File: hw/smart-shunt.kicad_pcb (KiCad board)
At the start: 2 copper layers, 80.3 x 50.3 mm, 36 parts, among them J1 V supply, J2 V bus <80, J3 V bus >80, J4 Conn_01x01_Female, J5 Conn_01x01_Female, J6 GND, U1 XL7005A, U2 INA228, U3 ESP-12F

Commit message: finished pcb
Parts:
- removed C6: 0.1uF, Capacitor_SMD:C_0805_2012Metric
- removed D1: SS310, Diode_SMD:D_SMA_Handsoldering
- removed J5: Conn_01x01_Female, TestPoint:TestPoint_Loop_D3.50mm_Drill0.9mm_Beaded
- removed J6: GND, TestPoint:TestPoint_Loop_D3.50mm_Drill0.9mm_Beaded
- removed R10: 33k, Resistor_SMD:R_0805_2012Metric
- removed R8, R9: 10k, Resistor_SMD:R_0805_2012Metric
- removed U3: ESP-12F, RF_Module:ESP-12E
- added C10: 1uF 100V, Capacitor_SMD:C_0805_2012Metric, F.Cu at (81.0, 99.6)
- added C11: 100nF, Capacitor_SMD:C_0805_2012Metric, F.Cu at (127.3, 103.8)
- added C7: 0.1uF, Capacitor_SMD:C_0805_2012Metric, F.Cu at (100.9, 93.0)
- added H1: MountingHole, MountingHole:MountingHole_2.2mm_M2, F.Cu at (80.5, 73.8)
- added H2: MountingHole, MountingHole:MountingHole_2.2mm_M2, F.Cu at (80.6, 107.3)
- added H3: MountingHole, MountingHole:MountingHole_2.2mm_M2, F.Cu at (127.8, 107.3)
- added H4: MountingHole, MountingHole:MountingHole_2.2mm_M2, F.Cu at (127.9, 73.9)
- added J10: Conn_01x02_Pin, Connector_PinHeader_2.54mm:PinHeader_1x02_P2.54mm_Vertical, F.Cu at (81.2, 90.3)
- added J7: Screw_Terminal_01x01, open-pe:Wuerth_PowerPlus_M5_Nut, F.Cu at (91.4, 81.3)
- added J8: Screw_Terminal_01x01, open-pe:Wuerth_PowerPlus_M5_Nut, F.Cu at (119.4, 81.3)
- added JP3: Jumper_3_Open, Jumper:SolderJumper-3_P1.3mm_Open_RoundedPad1.0x1.5mm, F.Cu at (93.5, 93.4)
- added JP4: SolderJumper_2_Open, PCM_Resistor_SMD_AKL:R_0402_1005Metric, F.Cu at (109.7, 105.2)
- added JP5: SolderJumper_2_Open, PCM_Resistor_SMD_AKL:R_0402_1005Metric, F.Cu at (109.7, 103.9)
- added JP6: SolderJumper_2_Open, PCM_Resistor_SMD_AKL:R_0402_1005Metric, F.Cu at (109.7, 102.6)
- added L2: LBR2012T101K, Inductor_SMD:L_0805_2012Metric, F.Cu at (107.1, 96.3)
- added PS1: MIE1W0505BGLVH-3R-Z, open-pe:CONV_MIE1W0505BGLVH-3R-Z, F.Cu at (117.9, 98.0)
- added R15: 10, Resistor_SMD:R_0805_2012Metric, F.Cu at (96.7, 88.9)
- added R16: 100, Resistor_SMD:R_0805_2012Metric, F.Cu at (98.1, 92.1)
- added R17: 10k, Resistor_SMD:R_0805_2012Metric, F.Cu at (100.3, 98.0)
- added R18: R_Shunt, Resistor_SMD:R_Shunt_Isabellenhuette_BVR4026, F.Cu at (104.2, 81.3)
- added TH1: Thermistor_NTC, PCM_Resistor_SMD_AKL:R_0402_1005Metric, F.Cu at (104.1, 76.7)
- added TH2: Thermistor_NTC, PCM_Resistor_SMD_AKL:R_0402_1005Metric, F.Cu at (104.1, 80.5)
- added U4: TPT7721-SO1R, Package_SO:SOP-8_3.9x4.9mm_P1.27mm, F.Cu at (124.2, 92.1)
- C2: value 33nF -> 100nF
- C5: value 100uF -> 22uF; footprint Capacitor_SMD:CP_Elec_8x10 -> Capacitor_SMD:CP_Elec_6.3x5.9
- J1: value V supply -> Conn_01x03_Socket; footprint TestPoint:TestPoint_Loop_D3.50mm_Drill0.9mm_Beaded -> Connector_PinHeader_2.54mm:PinHeader_1x03_P2.54mm_Vertical
- J2: value V bus <80 -> UEXT_Slave; footprint TestPoint:TestPoint_Loop_D3.50mm_Drill0.9mm_Beaded -> Connector_PinHeader_2.54mm:PinHeader_2x05_P2.54mm_Vertical
- J3: value V bus >80 -> UEXT_Slave2; footprint TestPoint:TestPoint_Loop_D3.50mm_Drill0.9mm_Beaded -> Connector_PinHeader_2.54mm:PinHeader_2x05_P2.54mm_Vertical
- J4: value Conn_01x01_Female -> Conn_01x02_Pin; footprint TestPoint:TestPoint_Loop_D3.50mm_Drill0.9mm_Beaded -> Connector_PinHeader_2.54mm:PinHeader_1x02_P2.54mm_Vertical
- JP1: value Jumper_3_Bridged12 -> Jumper_2_Open; footprint Jumper:SolderJumper-3_P1.3mm_Bridged2Bar12_Pad1.0x1.5mm -> Jumper:SolderJumper-2_P1.3mm_Open_RoundedPad1.0x1.5mm
- JP2: value Jumper_2_Open -> SolderJumper_2_Open; footprint Jumper:SolderJumper-2_P1.3mm_Bridged2Bar_Pad1.0x1.5mm -> PCM_Resistor_SMD_AKL:R_0402_1005Metric
- L1: value 100uH -> 22uH; footprint Inductor_SMD:L_Taiyo-Yuden_NR-60xx_HandSoldering -> Inductor_SMD:L_0805_2012Metric
- R1, R2: footprint Resistor_SMD:R_0805_2012Metric -> Resistor_THT:R_Axial_DIN0204_L3.6mm_D1.6mm_P7.62mm_Horizontal
- R7: value 33k -> 10; footprint Resistor_SMD:R_0805_2012Metric -> PCM_Resistor_SMD_AKL:R_0805_2012Metric
- TP1, TP2, TP3: footprint TestPoint:TestPoint_Loop_D3.50mm_Drill0.9mm_Beaded -> TestPoint:TestPoint_Pad_D1.0mm
- U1: value XL7005A -> TPT72616-SO1R
- moved R3 62.6 mm to (87.6, 93.3), turned to 90 degrees
- moved R1 61.8 mm to (87.6, 97.1), turned to 90 degrees
- moved J1 58.6 mm to (82.8, 102.9), turned to 90 degrees
- moved R2 56.7 mm to (89.8, 89.5), turned to -90 degrees
- moved R4 56.6 mm to (89.8, 93.3), turned to -90 degrees
- moved JP1 53.7 mm to (93.5, 89.2), turned to -90 degrees
- moved L1 50.2 mm to (80.0, 102.7), turned to 90 degrees
- moved R7 44.6 mm to (80.4, 96.3), turned to 90 degrees
- moved J2 41.1 mm to (106.7, 102.9), turned to -90 degrees
- moved JP2 38.0 mm to (109.7, 106.4)
- moved TP3 36.3 mm to (99.9, 90.1)
- moved J4 34.1 mm to (91.9, 105.4), turned to 180 degrees
- moved J3 29.3 mm to (124.5, 102.9), turned to -90 degrees
- moved C2 24.5 mm to (118.4, 94.1), turned to 180 degrees
- moved R11 23.2 mm to (118.4, 91.9), turned to 180 degrees
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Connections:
- C1 pad 2: Net-(TP2-Pad1) -> Net-(JP1-B)
- C2 pad 2: Net-(C2-Pad2) -> GND
- C3 pad 1: +3.3V -> Net-(U2-VS)
- C4 pad 1: +3.3V -> Net-(U2-VS)
- C5 pad 2: Net-(C5-Pad2) -> GND
- D2 pad 2: Alert -> +3.3V
- J1 pad 1: Net-(U1-Pad1) -> Net-(J1-Pin_1)
- J2 pad 1: Vbus -> +3.3V
- J3 pad 1: Net-(J3-Pad1) -> +3.3V2
- J4 pad 1: Net-(J4-Pad1) -> Net-(J4-Pin_1)
- JP1 pad 1: Vbus -> Net-(JP1-A)
- JP1 pad 2: Net-(JP1-Pad2) -> Net-(JP1-B)
- JP2 pad 1: Net-(JP2-Pad1) -> A0
- JP2 pad 2: Vbus -> GND
- L1 pad 1: Net-(D1-Pad1) -> Net-(J1-Pin_1)
- L1 pad 2: +3.3V -> Net-(C10-Pad2)
- R1 pad 1: Net-(JP2-Pad1) -> Net-(JP3-A)
- R1 pad 2: Net-(J3-Pad1) -> Vin
- R2 pad 2: Net-(JP2-Pad1) -> Net-(JP3-A)
- R3 pad 1: Net-(JP2-Pad1) -> Net-(JP3-A)
- R3 pad 2: Net-(J3-Pad1) -> Vin
- R4 pad 2: Net-(JP2-Pad1) -> Net-(JP3-A)
- R5 pad 1: Net-(J4-Pad1) -> Shunt+
- R6 pad 1: Net-(J5-Pad1) -> Shunt-
- R6 pad 2: Net-(TP2-Pad1) -> Net-(JP1-B)
- R7 pad 1: +3.3V -> Net-(C10-Pad2)
- R7 pad 2: Net-(C2-Pad2) -> Vin
- TP2 pad 1: Net-(TP2-Pad1) -> Net-(JP1-B)
- TP3 pad 1: Vbus -> Net-(U2-Vbus)
- U1 pad 1: Net-(U1-Pad1) -> +3.3V2
- U1 pad 2: Net-(D1-Pad1) -> SDA2
- U1 pad 3: Net-(C2-Pad2) -> SCL2
- U1 pad 4: Net-(C5-Pad2) -> GND2
- U1 pad 5: Net-(C5-Pad2) -> GND
- U1 pad 6: Net-(C5-Pad2) -> SCL
- U1 pad 7: Net-(C5-Pad2) -> SDA
- U1 pad 8: Net-(C5-Pad2) -> +3.3V
- U2 pad 2: GND -> A0
- U2 pad 6: +3.3V -> Net-(U2-VS)
- U2 pad 8: Vbus -> Net-(U2-Vbus)
- U2 pad 9: Net-(TP2-Pad1) -> Net-(JP1-B)
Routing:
- net +3.3V: track 0.00 -> 81.9 mm
- net SCL: track 0.00 -> 60.2 mm, vias 0 -> 2
- net SDA: track 0.00 -> 44.8 mm, vias 0 -> 1
- net Alert: track 0.00 -> 39.3 mm, vias 0 -> 2
- net Net-(J4-Pin_1): track 0.00 -> 36.6 mm, vias 0 -> 2
- net GND2: track 0.00 -> 33.9 mm
- net Net-(J4-Pin_2): track 0.00 -> 32.2 mm, vias 0 -> 1
- net +3.3V2: track 0.00 -> 28.2 mm
- net GND: track 0.00 -> 23.2 mm, vias 0 -> 3
- net Vin: track 0.00 -> 21.7 mm
- net Net-(JP1-B): track 0.00 -> 20.7 mm, vias 0 -> 2
- net A0: track 0.00 -> 14.9 mm, vias 0 -> 2
- net Alert2: track 0.00 -> 12.2 mm
- net SDA2: track 0.00 -> 11.4 mm, vias 0 -> 1
- net Net-(JP3-A): track 0.00 -> 10.6 mm
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- added copper zone on F.Cu, net GND
- added copper zone on B.Cu, net P+
- added copper zone on F.Cu, net P+
- added copper zone on B.Cu, net P-
- added copper zone on F.Cu, net P-
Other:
- board size 80.3 x 50.3 mm -> 50.8 x 37.1 mm
- board text added: "00"
- board text added: "01"
- board text added: "10"
- board text added: "11"
- board text added: "3.3V PSU"
- board text added: "NTC 10k"
- board text added: "UEXT (I2C)"
- board text added: "UEXT isolated"
- board text added: "i2c addr 100000xx"
- board text removed: "use double footprints for resistors (THT and SMD) add filter connectors"

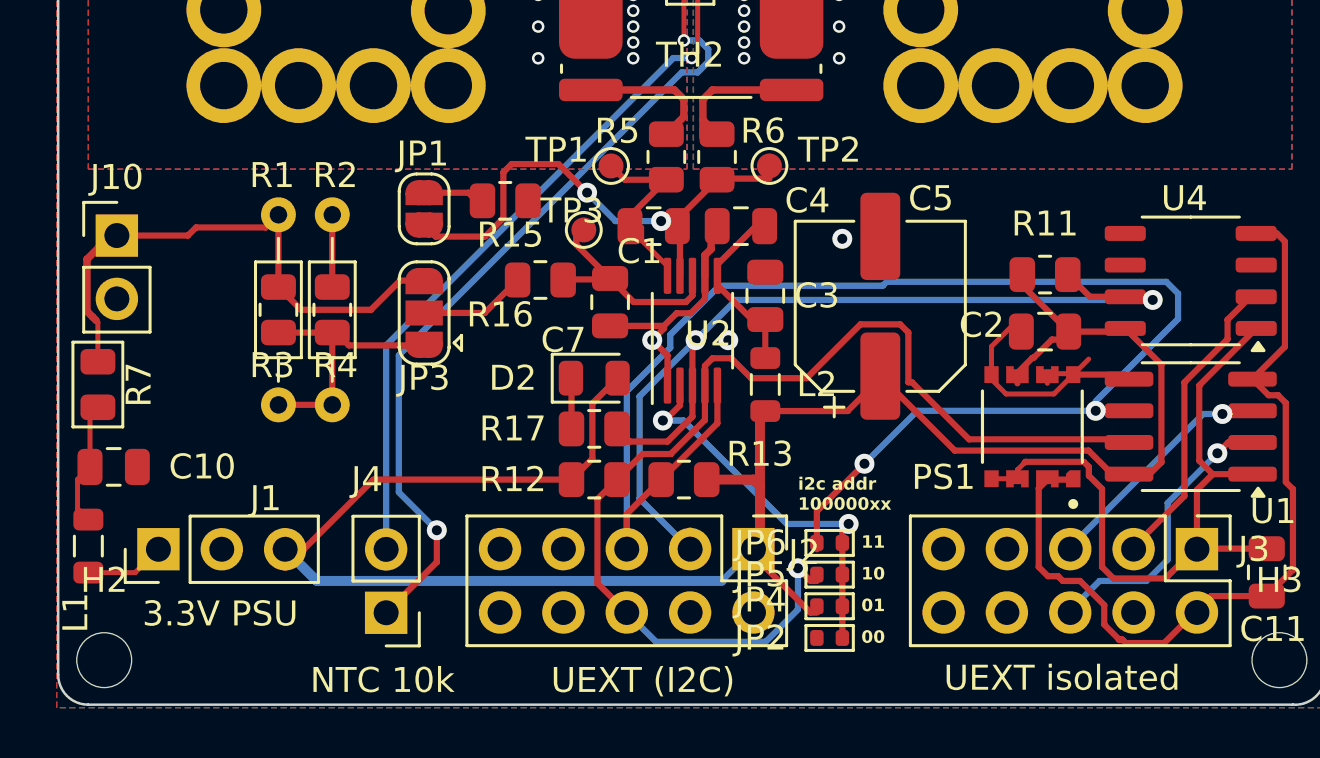
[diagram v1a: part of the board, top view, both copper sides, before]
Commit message: add battery connector and LDO
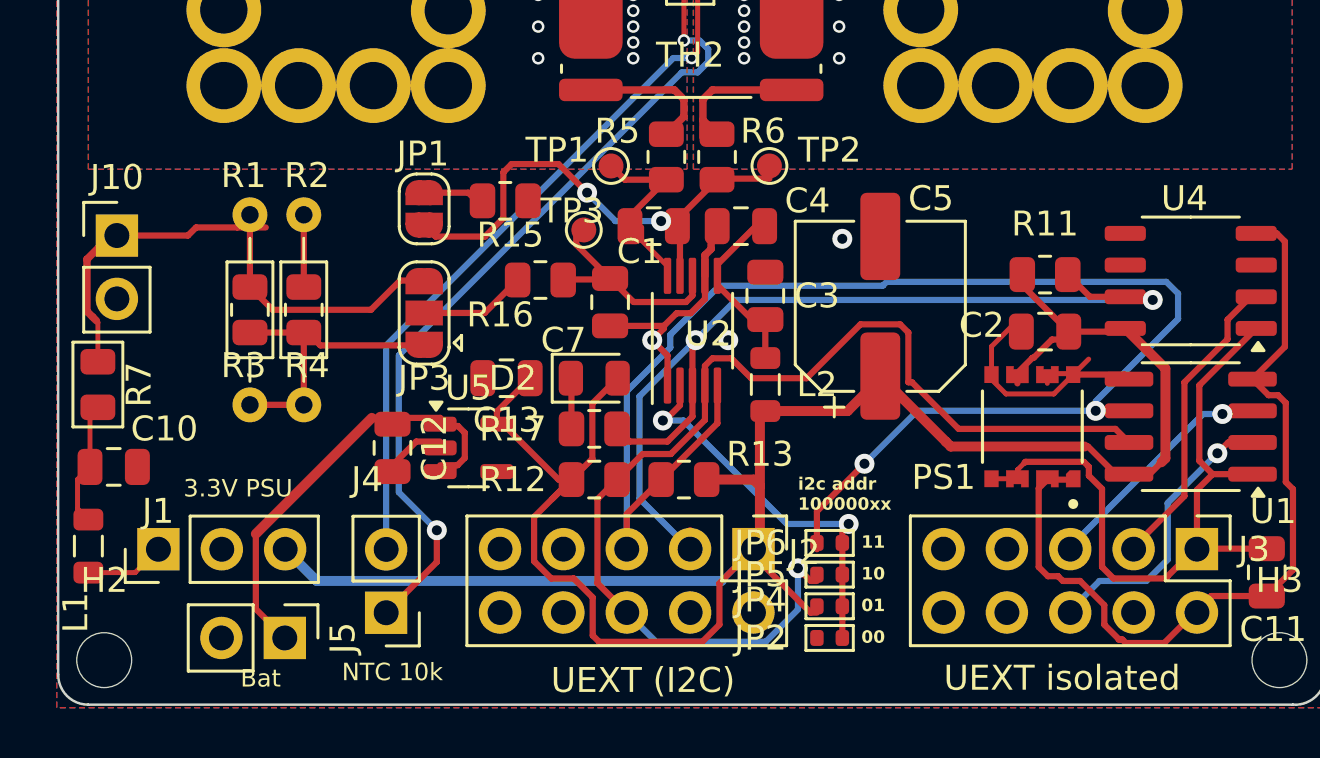
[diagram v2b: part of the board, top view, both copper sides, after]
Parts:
- added C12: 100nF, Capacitor_SMD:C_0805_2012Metric, F.Cu at (92.2, 98.8)
- added C13: 100nF, Capacitor_SMD:C_0805_2012Metric, F.Cu at (96.8, 96.0)
- added J5: Conn_01x02_Pin, Connector_PinHeader_2.54mm:PinHeader_1x02_P2.54mm_Vertical, F.Cu at (87.9, 106.4)
- added U5: TLV74033PDBVR, Package_TO_SOT_SMD:SOT-23-5, F.Cu at (95.2, 98.8)
- moved R1 1.14 mm to (86.5, 97.1)
- moved R2 1.14 mm to (88.6, 89.5)
- moved R3 1.14 mm to (86.5, 93.3)
- moved R4 1.14 mm to (88.6, 93.3)
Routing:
- net Net-(J5-Pin_1): track 0.00 -> 17.3 mm
- net +3.3V: track 81.9 -> 94.0 mm
- net GND: track 23.2 -> 25.5 mm
- net Vin: track 21.7 -> 22.8 mm
- net Net-(JP3-A): track 10.6 -> 11.7 mm
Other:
- board text added: "Bat"

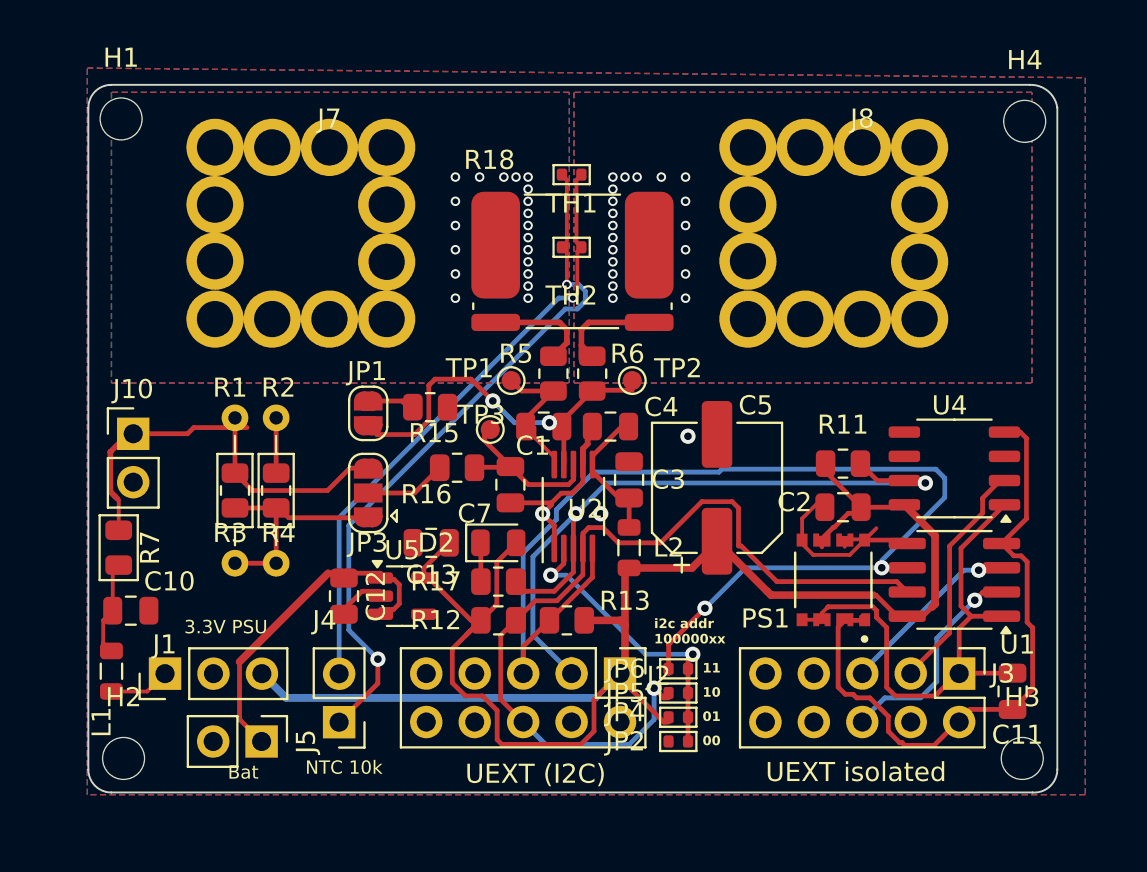
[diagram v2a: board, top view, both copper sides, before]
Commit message: hw: 2nd LDO, mounting holes
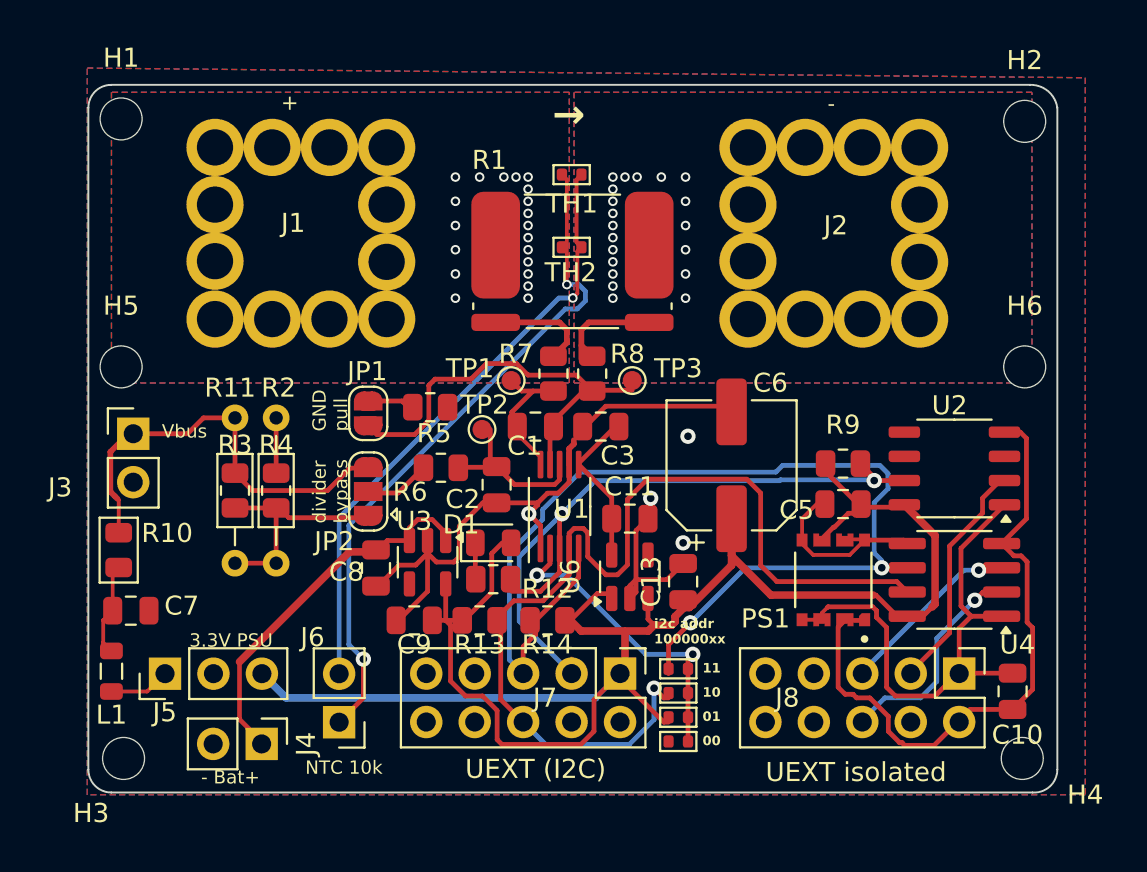
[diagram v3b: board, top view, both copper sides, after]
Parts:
- removed the C3 at (107.1, 92.7)
- removed L2: LBR2012T101K, Inductor_SMD:L_0805_2012Metric
- added C11: 1uF, Capacitor_SMD:C_0805_2012Metric, F.Cu at (107.2, 94.7)
- added C13: 1uF, Capacitor_SMD:C_0805_2012Metric, F.Cu at (110.0, 98.0)
- added H5: MountingHole, MountingHole:MountingHole_2.2mm_M2, F.Cu at (80.5, 86.8)
- added H6: MountingHole, MountingHole:MountingHole_2.2mm_M2, F.Cu at (127.9, 86.8)
- added U6: TLV74130PDBVR, Package_TO_SOT_SMD:SOT-23-5, F.Cu at (107.2, 97.8)
- C1: value 0.1uF -> 100nF
- C2: renamed from C7; value 0.1uF -> 100nF, 100V
- C3: renamed from C4; value 0.1uF -> 100nF
- moved R13 4.57 mm to (99.3, 100.1)
- moved C9 4.16 mm to (95.9, 100.1)
- moved R14 2.58 mm to (102.9, 100.1)
- moved C8 2.23 mm to (93.9, 97.3)
- moved U3 2.22 mm to (96.6, 97.0), turned to -90 degrees
- moved C6 1.40 mm to (112.5, 91.9)
- moved R6 0.85 mm to (97.3, 92.1)
- moved C2 0.72 mm to (100.2, 93.0)
- moved U1 0.72 mm to (103.5, 94.1)
- moved C3 0.51 mm to (105.7, 89.9)
- moved C1 0.44 mm to (102.2, 89.9)
- moved TP2 0.43 mm to (99.4, 90.1)
- moved R12 0.30 mm to (100.0, 97.9)
- moved D1 0.27 mm to (100.0, 96.0)
- moved C5 0.16 mm to (118.4, 94.0)
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- renumbered C11 to C10, C2 to C5, C5 to C6, C10 to C7, C12 to C8, C13 to C9, D2 to D1, H4 to H2, H2 to H3, H3 to H4, J7 to J1, J8 to J2, J10 to J3, J5 to J4, J1 to J5, J4 to J6, J2 to J7, J3 to J8, JP3 to JP2, JP4 to JP3, JP2 to JP4, JP6 to JP5, JP5 to JP6, R18 to R1, R7 to R10, R1 to R11, R17 to R12, R12 to R14, R15 to R5, R16 to R6, R5 to R7, R6 to R8, R11 to R9, TP3 to TP2, TP2 to TP3, U2 to U1, U4 to U2, U5 to U3, U1 to U4
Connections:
- net Net-(U2-VS) renamed +3V
- R13 pad 1: +3.3V -> SDA
- R13 pad 2: SCL -> +3.3V
- R14 pad 1: SDA -> +3.3V
- R14 pad 2: +3.3V -> SCL
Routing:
- net GND: track 25.5 -> 54.1 mm, vias 3 -> 4
- net SDA: track 44.8 -> 51.8 mm
- net SCL: track 60.2 -> 57.4 mm
- net +3.3V: track 94.0 -> 96.8 mm
- net Net-(J4-Pin_1): track 17.3 -> 20.1 mm
- net Alert: track 39.3 -> 37.1 mm
- net Net-(JP1-B): track 20.7 -> 22.7 mm, vias 2 -> 0
- net +3V: track 7.42 -> 8.62 mm
- net Vin: track 22.8 -> 21.7 mm
- net Vbus: track 3.79 -> 2.94 mm
- net A0: track 14.9 -> 15.6 mm
- net Net-(J6-Pin_1): track 36.6 -> 35.9 mm
- net Net-(U1-Vbus): track 9.16 -> 8.58 mm
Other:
- board text added: "+"
- board text added: "-"
- board text added: "- Bat+"
- board text added: "GND pull"
- board text added: "Vbus"
- board text added: "divider bypass"
- board text added: "→"
- board text removed: "Bat"

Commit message: etc
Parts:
- added J10: Conn_01x01, Connector_PinHeader_2.54mm:PinHeader_1x01_P2.54mm_Vertical, F.Cu at (100.4, 85.9)
- added J11: Conn_01x01, Connector_PinHeader_2.54mm:PinHeader_1x01_P2.54mm_Vertical, F.Cu at (107.9, 85.9)
- added JP7: Jumper_2_Open, open-pe:SolderJumper_0402_1005Metric, F.Cu at (103.1, 85.1)
- added JP8: Jumper_2_Open, open-pe:SolderJumper_0402_1005Metric, F.Cu at (105.2, 85.1)
- added R15: WSK12161L000FEA, open-pe:SMT_61L000FEA_VIS, F.Cu at (104.2, 81.3)
- added R16: WSK12161L000FEA, open-pe:CSM3637_1-2mOHM_VIS, F.Cu at (104.2, 79.3)
- JP2: value Jumper_3_Open -> VbusSel
- JP3, JP4, JP5, JP6: footprint PCM_Resistor_SMD_AKL:R_0402_1005Metric -> open-pe:SolderJumper_0402_1005Metric
- moved TH1 3.01 mm to (104.2, 73.7)
- moved TH2 2.87 mm to (104.1, 77.7), turned to -90 degrees
- moved R1 1.02 mm to (104.2, 80.2)
- moved TP1 0.98 mm to (100.2, 88.1)
- moved TP3 0.68 mm to (107.8, 88.0)
- moved JP4 0.25 mm to (109.7, 106.7)
- moved JP5 0.25 mm to (109.7, 102.9)
- moved JP6 0.25 mm to (109.7, 104.1)
- moved JP3 0.25 mm to (109.7, 105.4)
- moved R7 0.24 mm to (103.1, 87.4)
- moved R8 0.24 mm to (105.2, 87.4)
- moved C3 0.15 mm to (105.7, 90.1)
- moved C1 0.15 mm to (102.2, 90.1)
- moved U1 0.13 mm to (103.5, 94.2)
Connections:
- R1 pad 2: Shunt+ -> Net-(JP7-A)
- R1 pad 3: Shunt- -> Net-(JP8-A)
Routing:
- net Net-(J6-Pin_2): track 32.2 -> 38.6 mm
- net Net-(JP8-A): track 0.00 -> 3.67 mm
- net Net-(JP7-A): track 0.00 -> 3.64 mm
- net Net-(J6-Pin_1): track 35.9 -> 38.6 mm
- net Shunt-: track 6.03 -> 4.33 mm
- net A0: track 15.6 -> 17.3 mm
- net Shunt+: track 5.57 -> 4.32 mm
- net GND: track 54.1 -> 55.3 mm
- net Net-(U1-Vbus): track 8.58 -> 9.62 mm
- net SDA: track 51.8 -> 52.7 mm
- net Net-(U1-Vin+): track 7.14 -> 7.70 mm
- net P-: vias 20 -> 24
- net P+: vias 20 -> 25
